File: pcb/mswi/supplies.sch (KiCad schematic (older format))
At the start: 11 parts, among them U501 LM7805

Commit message: Schematics Annotated
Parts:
- gave numbers to parts that had none: 5
- renumbered C501 to C601, C502 to C602, C503 to C605, C504 to C606, F501 to F601, U501 to U601
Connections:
- net +18V_OUT: no longer names the net of C601.1, C602.1, C603.1, F601.2, R601.1, U601.1 (VI)
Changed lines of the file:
@@
 $Descr A4 11693 8268
 encoding utf-8
-Sheet 4 6
+Sheet 6 6
 Title ""
 Date ""
@@
 $EndDescr
 $Comp
-L Regulator_Linear:LM7805_TO220 U501
+L Regulator_Linear:LM7805_TO220 U601
 U 1 1 5A007B62
 P 5900 3950
-AR Path="/5AACFFEF/5A007B62" Ref="U501"  Part="1"
+AR Path="/5AACFFEF/5A007B62" Ref="U601"  Part="1"
 AR Path="/5DDD6AD9/5A007B62" Ref="U?"  Part="1"
 AR Path="/5DDDDD89/5A007B62" Ref="U?"  Part="1"
-F 0 "U?" H 5750 4075 50  0000 C CNN
+F 0 "U601" H 5750 4075 50  0000 C CNN
 F 1 "LM7805" H 5900 4100 50  0000 L CNN
 F 2 "KicadZeniteSolarLibrary18:TO-220-3_Horizontal_TabDown_SMD" H 5900 4175 50  0001 C CIN
@@
 +5V_OUT
 $Comp
-L Device:CP1_Small C501
+L Device:CP1_Small C601
 U 1 1 5A008895
 P 4900 4400
-AR Path="/5AACFFEF/5A008895" Ref="C501"  Part="1"
+AR Path="/5AACFFEF/5A008895" Ref="C601"  Part="1"
 AR Path="/5DDD6AD9/5A008895" Ref="C?"  Part="1"
 AR Path="/5DDDDD89/5A008895" Ref="C?"  Part="1"
-F 0 "C?" H 4910 4470 50  0000 L CNN
+F 0 "C601" H 4910 4470 50  0000 L CNN
 F 1 "1uF" H 4910 4320 50  0000 L CNN
 F 2 "Capacitor_Tantalum_SMD:CP_EIA-6032-20_AVX-F_Pad2.25x2.35mm_HandSolder" H 4900 4400 50  0001 C CNN
@@
 $EndComp
 $Comp
-L Device:C_Small C502
+L Device:C_Small C602
 U 1 1 5A00899A
 P 5200 4400
-AR Path="/5AACFFEF/5A00899A" Ref="C502"  Part="1"
+AR Path="/5AACFFEF/5A00899A" Ref="C602"  Part="1"
 AR Path="/5DDD6AD9/5A00899A" Ref="C?"  Part="1"
 AR Path="/5DDDDD89/5A00899A" Ref="C?"  Part="1"
-F 0 "C?" H 5210 4470 50  0000 L CNN
+F 0 "C602" H 5210 4470 50  0000 L CNN
 F 1 "100nF" H 5210 4320 50  0000 L CNN
 F 2 "Capacitor_SMD:C_0805_2012Metric_Pad1.15x1.40mm_HandSolder" H 5200 4400 50  0001 C CNN
@@
 +18V_IN
 $Comp
-L Device:C_Small C503
+L Device:C_Small C605
 U 1 1 5A00B18A
 P 6650 4400
-AR Path="/5AACFFEF/5A00B18A" Ref="C503"  Part="1"
+AR Path="/5AACFFEF/5A00B18A" Ref="C605"  Part="1"
 AR Path="/5DDD6AD9/5A00B18A" Ref="C?"  Part="1"
 AR Path="/5DDDDD89/5A00B18A" Ref="C?"  Part="1"
-F 0 "C?" H 6660 4470 50  0000 L CNN
+F 0 "C605" H 6660 4470 50  0000 L CNN
 F 1 "100nF" H 6660 4320 50  0000 L CNN
 F 2 "Capacitor_SMD:C_0805_2012Metric_Pad1.15x1.40mm_HandSolder" H 6650 4400 50  0001 C CNN
@@
 $EndComp
 $Comp
-L Device:CP1_Small C504
+L Device:CP1_Small C606
 U 1 1 5AAD0D5C
 P 7000 4400
-AR Path="/5AACFFEF/5AAD0D5C" Ref="C504"  Part="1"
+AR Path="/5AACFFEF/5AAD0D5C" Ref="C606"  Part="1"
 AR Path="/5DDD6AD9/5AAD0D5C" Ref="C?"  Part="1"
 AR Path="/5DDDDD89/5AAD0D5C" Ref="C?"  Part="1"
-F 0 "C?" H 7010 4470 50  0000 L CNN
+F 0 "C606" H 7010 4470 50  0000 L CNN
 F 1 "10uF" H 7010 4320 50  0000 L CNN
 F 2 "Capacitor_Tantalum_SMD:CP_EIA-6032-20_AVX-F_Pad2.25x2.35mm_HandSolder" H 7000 4400 50  0001 C CNN
@@
 $EndComp
 $Comp
-L Device:Fuse_Small F501
+L Device:Fuse_Small F601
 U 1 1 5AB12173
 P 3700 3950
-AR Path="/5AACFFEF/5AB12173" Ref="F501"  Part="1"
+AR Path="/5AACFFEF/5AB12173" Ref="F601"  Part="1"
 AR Path="/5DDD6AD9/5AB12173" Ref="F?"  Part="1"
 AR Path="/5DDDDD89/5AB12173" Ref="F?"  Part="1"
-F 0 "F?" H 3700 3890 50  0000 C CNN
+F 0 "F601" H 3700 3890 50  0000 C CNN
 F 1 "500mA" H 3700 4010 50  0000 C CNN
 F 2 "Fuse:Fuse_1206_3216Metric_Pad1.42x1.75mm_HandSolder" H 3700 3950 50  0001 C CNN
@@
 Wire Wire Line
 	6650 3950 6650 4300
-Text HLabel 6650 3550 2    60   Input ~ 0
-+18V_OUT
-Wire Wire Line
-	5200 3550 5200 3950
-Wire Wire Line
-	5200 3550 6650 3550
-Connection ~ 5200 3550
-Wire Wire Line
-	5200 3450 5200 3550
-$Comp
-L power:PWR_FLAG #FLG0501
+$Comp
+L power:PWR_FLAG #FLG0601
 U 1 1 5BE75359
-P 5200 3450
-AR Path="/5AACFFEF/5BE75359" Ref="#FLG0501"  Part="1"
+P 5200 3850
+AR Path="/5AACFFEF/5BE75359" Ref="#FLG0601"  Part="1"
 AR Path="/5DDD6AD9/5BE75359" Ref="#FLG?"  Part="1"
 AR Path="/5DDDDD89/5BE75359" Ref="#FLG?"  Part="1"
-F 0 "#FLG?" H 5200 3525 50  0001 C CNN
-F 1 "PWR_FLAG" H 5200 3650 50  0000 C CNN
-F 2 "" H 5200 3450 50  0001 C CNN
-F 3 "~" H 5200 3450 50  0001 C CNN
-	1    5200 3450
-	1    0    0    -1
-$EndComp
-$Comp
-L power:PWR_FLAG #FLG0502
+F 0 "#FLG0601" H 5200 3925 50  0001 C CNN
+F 1 "PWR_FLAG" H 5200 4050 50  0000 C CNN
+F 2 "" H 5200 3850 50  0001 C CNN
+F 3 "~" H 5200 3850 50  0001 C CNN
+	1    5200 3850
+	1    0    0    -1
+$EndComp
+$Comp
+L power:PWR_FLAG #FLG0602
 U 1 1 5BE753AF
 P 5200 4900
-AR Path="/5AACFFEF/5BE753AF" Ref="#FLG0502"  Part="1"
+AR Path="/5AACFFEF/5BE753AF" Ref="#FLG0602"  Part="1"
 AR Path="/5DDD6AD9/5BE753AF" Ref="#FLG?"  Part="1"
 AR Path="/5DDDDD89/5BE753AF" Ref="#FLG?"  Part="1"
-F 0 "#FLG?" H 5200 4975 50  0001 C CNN
+F 0 "#FLG0602" H 5200 4975 50  0001 C CNN
 F 1 "PWR_FLAG" H 5200 5100 50  0000 C CNN
 F 2 "" H 5200 4900 50  0001 C CNN
@@
 	4050 4800 4100 4800
 $Comp
-L Device:Q_NMOS_GSD Q?
+L Device:Q_NMOS_GSD Q601
 U 1 1 5D9E3E7E
 P 3850 4700
-AR Path="/5AACFFEF/5D9E3E7E" Ref="Q?"  Part="1"
+AR Path="/5AACFFEF/5D9E3E7E" Ref="Q601"  Part="1"
 AR Path="/5DDD6AD9/5D9E3E7E" Ref="Q?"  Part="1"
 AR Path="/5DDDDD89/5D9E3E7E" Ref="Q?"  Part="1"
-F 0 "Q?" V 3400 4600 50  0000 C CNN
+F 0 "Q601" V 3400 4600 50  0000 C CNN
 F 1 "Q_NMOS_GSD" V 3750 4450 50  0000 C CNN
 F 2 "" H 4050 4800 50  0001 C CNN
@@
 	4100 4800 4900 4800
 $Comp
-L Device:R_Small R?
+L Device:R_Small R601
 U 1 1 5D9E9D52
 P 4100 4150
-AR Path="/5AACFFEF/5D9E9D52" Ref="R?"  Part="1"
+AR Path="/5AACFFEF/5D9E9D52" Ref="R601"  Part="1"
 AR Path="/5DDD6AD9/5D9E9D52" Ref="R?"  Part="1"
 AR Path="/5DDDDD89/5D9E9D52" Ref="R?"  Part="1"
-F 0 "R?" H 4200 4200 50  0000 L CNN
+F 0 "R601" H 4200 4200 50  0000 L CNN
 F 1 "1M" H 4200 4150 50  0000 L CNN
 F 2 "" H 4100 4150 50  0001 C CNN
@@
 $EndComp
 $Comp
-L Device:D_Zener_Small D?
+L Device:D_Zener_Small D601
 U 1 1 5D9EA99D
 P 4100 4600
-AR Path="/5AACFFEF/5D9EA99D" Ref="D?"  Part="1"
+AR Path="/5AACFFEF/5D9EA99D" Ref="D601"  Part="1"
 AR Path="/5DDD6AD9/5D9EA99D" Ref="D?"  Part="1"
 AR Path="/5DDDDD89/5D9EA99D" Ref="D?"  Part="1"
-F 0 "D?" V 4000 4700 50  0000 L CNN
+F 0 "D601" V 4000 4700 50  0000 L CNN
 F 1 "MMSZ5240BT1" V 4100 4700 50  0000 L CNN
 F 2 "" V 4100 4600 50  0001 C CNN
@@
 	3400 4800 3650 4800
 $Comp
-L Device:C_Small C?
+L Device:C_Small C603
 U 1 1 5D9EFA18
 P 5500 4400
-AR Path="/5AACFFEF/5D9EFA18" Ref="C?"  Part="1"
+AR Path="/5AACFFEF/5D9EFA18" Ref="C603"  Part="1"
 AR Path="/5DDD6AD9/5D9EFA18" Ref="C?"  Part="1"
 AR Path="/5DDDDD89/5D9EFA18" Ref="C?"  Part="1"
-F 0 "C?" H 5510 4470 50  0000 L CNN
+F 0 "C603" H 5510 4470 50  0000 L CNN
 F 1 "100nF" H 5510 4320 50  0000 L CNN
 F 2 "Capacitor_SMD:C_0805_2012Metric_Pad1.15x1.40mm_HandSolder" H 5500 4400 50  0001 C CNN
@@
 	5500 4800 5900 4800
 $Comp
-L Device:C_Small C?
+L Device:C_Small C604
 U 1 1 5D9F17B7
 P 6300 4400
-AR Path="/5AACFFEF/5D9F17B7" Ref="C?"  Part="1"
+AR Path="/5AACFFEF/5D9F17B7" Ref="C604"  Part="1"
 AR Path="/5DDD6AD9/5D9F17B7" Ref="C?"  Part="1"
 AR Path="/5DDDDD89/5D9F17B7" Ref="C?"  Part="1"
-F 0 "C?" H 6310 4470 50  0000 L CNN
+F 0 "C604" H 6310 4470 50  0000 L CNN
 F 1 "100nF" H 6310 4320 50  0000 L CNN
 F 2 "Capacitor_SMD:C_0805_2012Metric_Pad1.15x1.40mm_HandSolder" H 6300 4400 50  0001 C CNN
@@
 Wire Wire Line
 	6300 4800 6650 4800
+Wire Wire Line
+	5200 3850 5200 3950
 $EndSCHEMATC

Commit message: Footprints associated
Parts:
- C601: footprint Capacitor_Tantalum_SMD:CP_EIA-6032-20_AVX-F_Pad2.25x2.35mm_HandSolder -> Capacitor_SMD:C_0805_2012Metric_Pad1.15x1.40mm_HandSolder; symbol Device:CP1_Small -> Device:C_Small
- D601: footprint (none) -> Diode_SMD:D_SOD-123
- Q601: value Q_NMOS_GSD -> si2308cds; footprint (none) -> Package_TO_SOT_SMD:SOT-23
- R601: footprint (none) -> Resistor_SMD:R_0805_2012Metric_Pad1.15x1.40mm_HandSolder
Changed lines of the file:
@@
 +5V_OUT
 $Comp
-L Device:CP1_Small C601
+L Device:C_Small C601
 U 1 1 5A008895
 P 4900 4400
@@
 F 0 "C601" H 4910 4470 50  0000 L CNN
 F 1 "1uF" H 4910 4320 50  0000 L CNN
-F 2 "Capacitor_Tantalum_SMD:CP_EIA-6032-20_AVX-F_Pad2.25x2.35mm_HandSolder" H 4900 4400 50  0001 C CNN
+F 2 "Capacitor_SMD:C_0805_2012Metric_Pad1.15x1.40mm_HandSolder" H 4900 4400 50  0001 C CNN
 F 3 "" H 4900 4400 50  0001 C CNN
 	1    4900 4400
@@
 AR Path="/5DDDDD89/5D9E3E7E" Ref="Q?"  Part="1"
 F 0 "Q601" V 3400 4600 50  0000 C CNN
-F 1 "Q_NMOS_GSD" V 3750 4450 50  0000 C CNN
-F 2 "" H 4050 4800 50  0001 C CNN
+F 1 "si2308cds" V 3750 4450 50  0000 C CNN
+F 2 "Package_TO_SOT_SMD:SOT-23" H 4050 4800 50  0001 C CNN
 F 3 "~" H 3850 4700 50  0001 C CNN
 	1    3850 4700
@@
 AR Path="/5DDDDD89/5D9E9D52" Ref="R?"  Part="1"
 F 0 "R601" H 4200 4200 50  0000 L CNN
-F 1 "1M" H 4200 4150 50  0000 L CNN
-F 2 "" H 4100 4150 50  0001 C CNN
+F 1 "1M" H 4200 4100 50  0000 L CNN
+F 2 "Resistor_SMD:R_0805_2012Metric_Pad1.15x1.40mm_HandSolder" H 4100 4150 50  0001 C CNN
 F 3 "~" H 4100 4150 50  0001 C CNN
 	1    4100 4150
@@
 F 0 "D601" V 4000 4700 50  0000 L CNN
 F 1 "MMSZ5240BT1" V 4100 4700 50  0000 L CNN
-F 2 "" V 4100 4600 50  0001 C CNN
+F 2 "Diode_SMD:D_SOD-123" V 4100 4600 50  0001 C CNN
 F 3 "~" V 4100 4600 50  0001 C CNN
 F 4 "10V" V 4200 4700 50  0000 L CNN "Voltage"

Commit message: TVS added
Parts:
- added D602: 400W 24VDC, Diode_SMD:D_SMA, symbol Device:D_TVS
- F601: Model (none) -> 0ZCJ0050AF2E; Mouser (none) -> https://br.mouser.com/ProductDetail/Bel-Fuse/0ZCJ0050AF2E?q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
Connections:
- net GND_IN: now also D602.2 (A2)
- net +18V: now reaches C601.1, C602.1, C603.1, F601.2, R601.1, U601.1 (VI)
- net +18V: now also D602.1 (A1)
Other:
- note added: "TVS:\nhttps://m.littelfuse.com/~~/media/electronics/application_notes/littelfuse_tvs_diode_overview_application_note.pdf.pdf"
- moved on the sheet: F601
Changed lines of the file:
@@
 	1    0    0    -1
 $EndComp
-Text HLabel 3400 4800 0    60   Input ~ 0
+Text HLabel 3050 4800 0    60   Input ~ 0
 GND_IN
 Text HLabel 7300 3950 2    60   Output ~ 0
@@
 	1    0    0    -1
 $EndComp
-Text HLabel 3400 3950 0    60   Input ~ 0
+Text HLabel 3050 3950 0    60   Input ~ 0
 +18V_IN
 $Comp
@@
 L Device:Fuse_Small F601
 U 1 1 5AB12173
-P 3700 3950
+P 3350 3950
 AR Path="/5AACFFEF/5AB12173" Ref="F601"  Part="1"
 AR Path="/5DDD6AD9/5AB12173" Ref="F?"  Part="1"
 AR Path="/5DDDDD89/5AB12173" Ref="F?"  Part="1"
-F 0 "F601" H 3700 3890 50  0000 C CNN
-F 1 "500mA" H 3700 4010 50  0000 C CNN
-F 2 "Fuse:Fuse_1206_3216Metric_Pad1.42x1.75mm_HandSolder" H 3700 3950 50  0001 C CNN
-F 3 "https://www.mouser.com/datasheet/2/643/0ZCJ_Nov2016-1132002.pdf" H 3700 3950 50  0001 C CNN
-	1    3700 3950
+F 0 "F601" H 3350 3890 50  0000 C CNN
+F 1 "500mA" H 3350 4010 50  0000 C CNN
+F 2 "Fuse:Fuse_1206_3216Metric_Pad1.42x1.75mm_HandSolder" H 3350 3950 50  0001 C CNN
+F 3 "https://www.mouser.com/datasheet/2/643/0ZCJ_Nov2016-1132002.pdf" H 3350 3950 50  0001 C CNN
+F 4 "https://br.mouser.com/ProductDetail/Bel-Fuse/0ZCJ0050AF2E?qs=%2Fha2pyFadugaoNql5zaJPtCzxaRCuZne0%252BGltuyizoH09DOBIA3TDQ%3D%3D" H 3350 3950 50  0001 C CNN "Mouser"
+F 5 "0ZCJ0050AF2E" H 3350 3950 50  0001 C CNN "Model"
+	1    3350 3950
 	1    0    0    -1
 $EndComp
@@
 	4900 3950 4900 4300
 Wire Wire Line
-	3800 3950 4100 3950
+	3450 3950 3600 3950
 Wire Wire Line
 	4900 3950 5200 3950
@@
 	7000 4800 7300 4800
 Wire Wire Line
-	3400 3950 3600 3950
+	3050 3950 3250 3950
 Wire Wire Line
 	4050 4800 4100 4800
@@
 AR Path="/5DDD6AD9/5D9E3E7E" Ref="Q?"  Part="1"
 AR Path="/5DDDDD89/5D9E3E7E" Ref="Q?"  Part="1"
-F 0 "Q601" V 3400 4600 50  0000 C CNN
-F 1 "si2308cds" V 3750 4450 50  0000 C CNN
+F 0 "Q601" V 4100 4700 50  0000 C CNN
+F 1 "si2308cds" V 4200 4700 50  0000 C CNN
 F 2 "Package_TO_SOT_SMD:SOT-23" H 4050 4800 50  0001 C CNN
 F 3 "~" H 3850 4700 50  0001 C CNN
@@
 Connection ~ 4100 3950
 Wire Wire Line
-	4100 3950 4900 3950
-Wire Wire Line
 	4100 4700 4100 4800
 Wire Wire Line
@@
 	4100 4400 4100 4500
 Wire Wire Line
-	3400 4800 3650 4800
+	3050 4800 3600 4800
 $Comp
 L Device:C_Small C603
@@
 Wire Wire Line
 	5200 3850 5200 3950
+Wire Wire Line
+	4100 3950 4900 3950
+Text Label 4400 3950 0    50   ~ 0
++18V
+$Comp
+L Device:D_TVS D602
+U 1 1 5DD19DD4
+P 3600 4400
+F 0 "D602" V 3550 4600 50  0000 R CNN
+F 1 "400W 24VDC" V 3650 4950 50  0000 R CNN
+F 2 "Diode_SMD:D_SMA" H 3600 4400 50  0001 C CNN
+F 3 "https://www.mouser.com/datasheet/2/445/824501241-952945.pdf" H 3600 4400 50  0001 C CNN
+F 4 "https://br.mouser.com/ProductDetail/Wurth-Elektronik/824501241?qs=%2Fha2pyFadujZKBgF5S1ldkLPpipTn8KXCRHX4IsQDUlguH4XSGuxlw%3D%3D" V 3600 4400 50  0001 C CNN "Mouser"
+	1    3600 4400
+	0    -1   1    0
+$EndComp
+Wire Wire Line
+	3600 4250 3600 3950
+Connection ~ 3600 3950
+Wire Wire Line
+	3600 3950 4100 3950
+Wire Wire Line
+	3600 4550 3600 4800
+Connection ~ 3600 4800
+Wire Wire Line
+	3600 4800 3650 4800
+Text Notes 3400 5350 0    39   ~ 0
+TVS:\nhttps://m.littelfuse.com/~~/media/electronics/application_notes/littelfuse_tvs_diode_overview_application_note.pdf.pdf
 $EndSCHEMATC

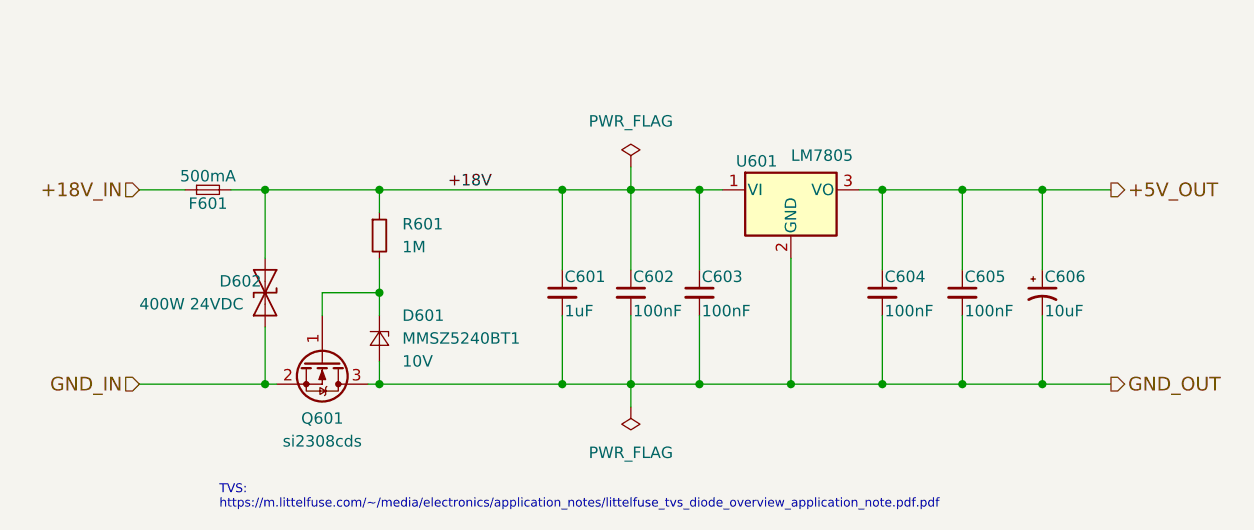
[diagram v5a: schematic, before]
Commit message: Routing done. Needs rework to fabrication
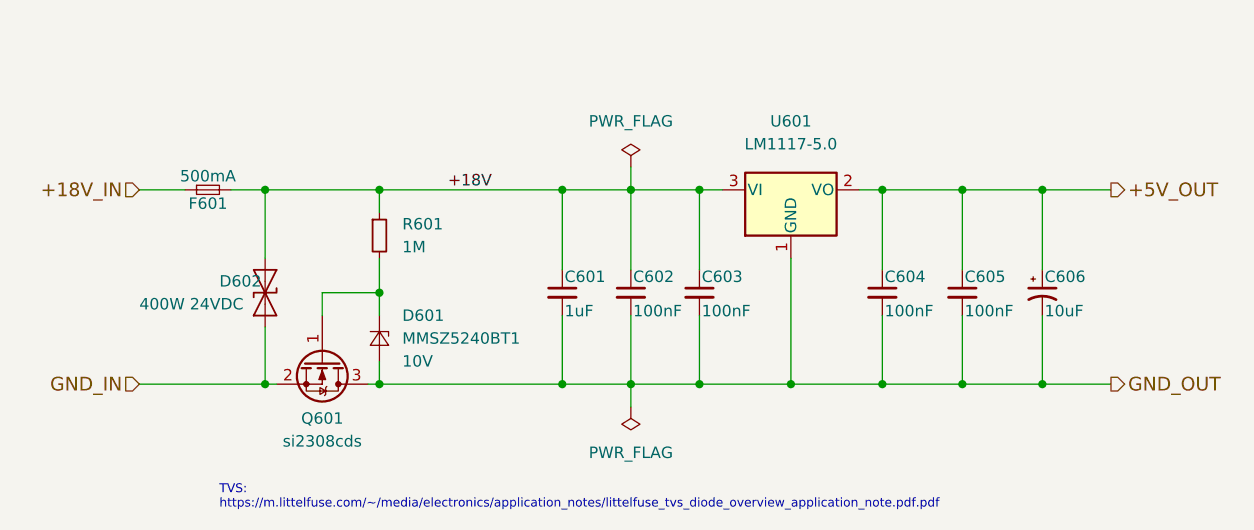
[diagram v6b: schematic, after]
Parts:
- removed U601: LM7805, KicadZeniteSolarLibrary18:TO-220-3_Horizontal_TabDown_SMD, symbol Regulator_Linear:LM7805_TO220
- added U601: LM1117-5.0, Package_TO_SOT_SMD:SOT-223-3_TabPin2, symbol Regulator_Linear:LM1117-5.0
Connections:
- net +18V: now also U601.3 (VI)
- net +5V_OUT: now also U601.2 (VO)
- net GND_OUT: now also U601.1 (GND)
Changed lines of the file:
@@
 Comment4 ""
 $EndDescr
-$Comp
-L Regulator_Linear:LM7805_TO220 U601
-U 1 1 5A007B62
-P 5900 3950
-AR Path="/5AACFFEF/5A007B62" Ref="U601"  Part="1"
-AR Path="/5DDD6AD9/5A007B62" Ref="U?"  Part="1"
-AR Path="/5DDDDD89/5A007B62" Ref="U?"  Part="1"
-F 0 "U601" H 5750 4075 50  0000 C CNN
-F 1 "LM7805" H 5900 4100 50  0000 L CNN
-F 2 "KicadZeniteSolarLibrary18:TO-220-3_Horizontal_TabDown_SMD" H 5900 4175 50  0001 C CIN
-F 3 "https://www.sparkfun.com/datasheets/Components/LM7805.pdf" H 5900 3900 50  0001 C CNN
-	1    5900 3950
-	1    0    0    -1
-$EndComp
 Text HLabel 3050 4800 0    60   Input ~ 0
 GND_IN
@@
 Text Notes 3400 5350 0    39   ~ 0
 TVS:\nhttps://m.littelfuse.com/~~/media/electronics/application_notes/littelfuse_tvs_diode_overview_application_note.pdf.pdf
+$Comp
+L Regulator_Linear:LM1117-5.0 U601
+U 1 1 5DA67007
+P 5900 3950
+F 0 "U601" H 5900 4250 50  0000 C CNN
+F 1 "LM1117-5.0" H 5900 4150 50  0000 C CNN
+F 2 "Package_TO_SOT_SMD:SOT-223-3_TabPin2" H 5900 3950 50  0001 C CNN
+F 3 "http://www.ti.com/lit/ds/symlink/lm1117.pdf" H 5900 3950 50  0001 C CNN
+	1    5900 3950
+	1    0    0    -1
+$EndComp
 $EndSCHEMATC
